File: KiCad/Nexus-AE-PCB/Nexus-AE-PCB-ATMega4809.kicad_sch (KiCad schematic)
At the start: 1 part, among them U1 ATmega4809-A

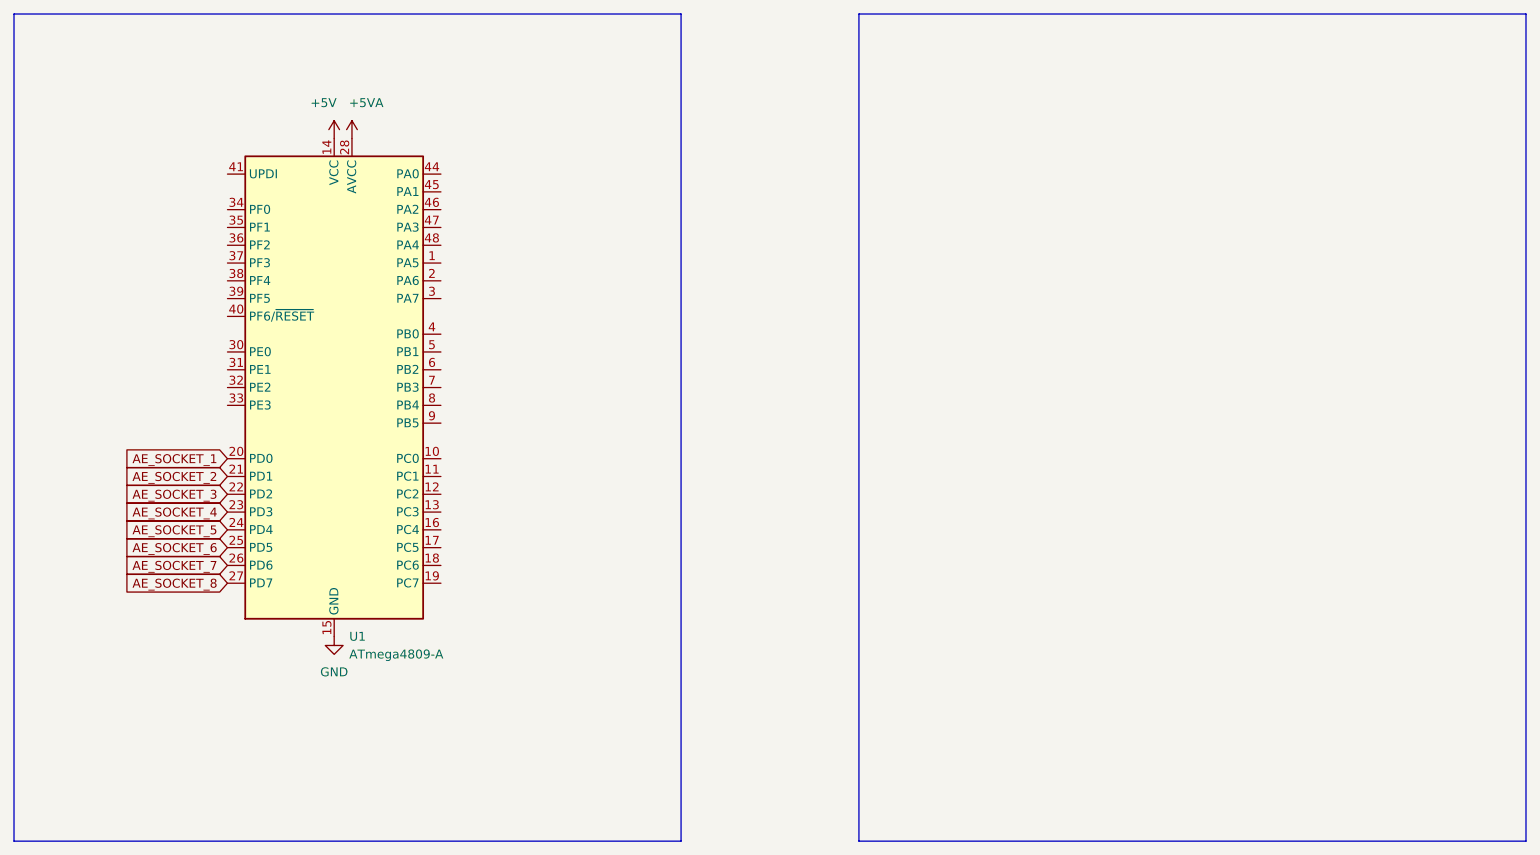
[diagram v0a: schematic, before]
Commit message: PCB and schmeatic are both approx 90% complete
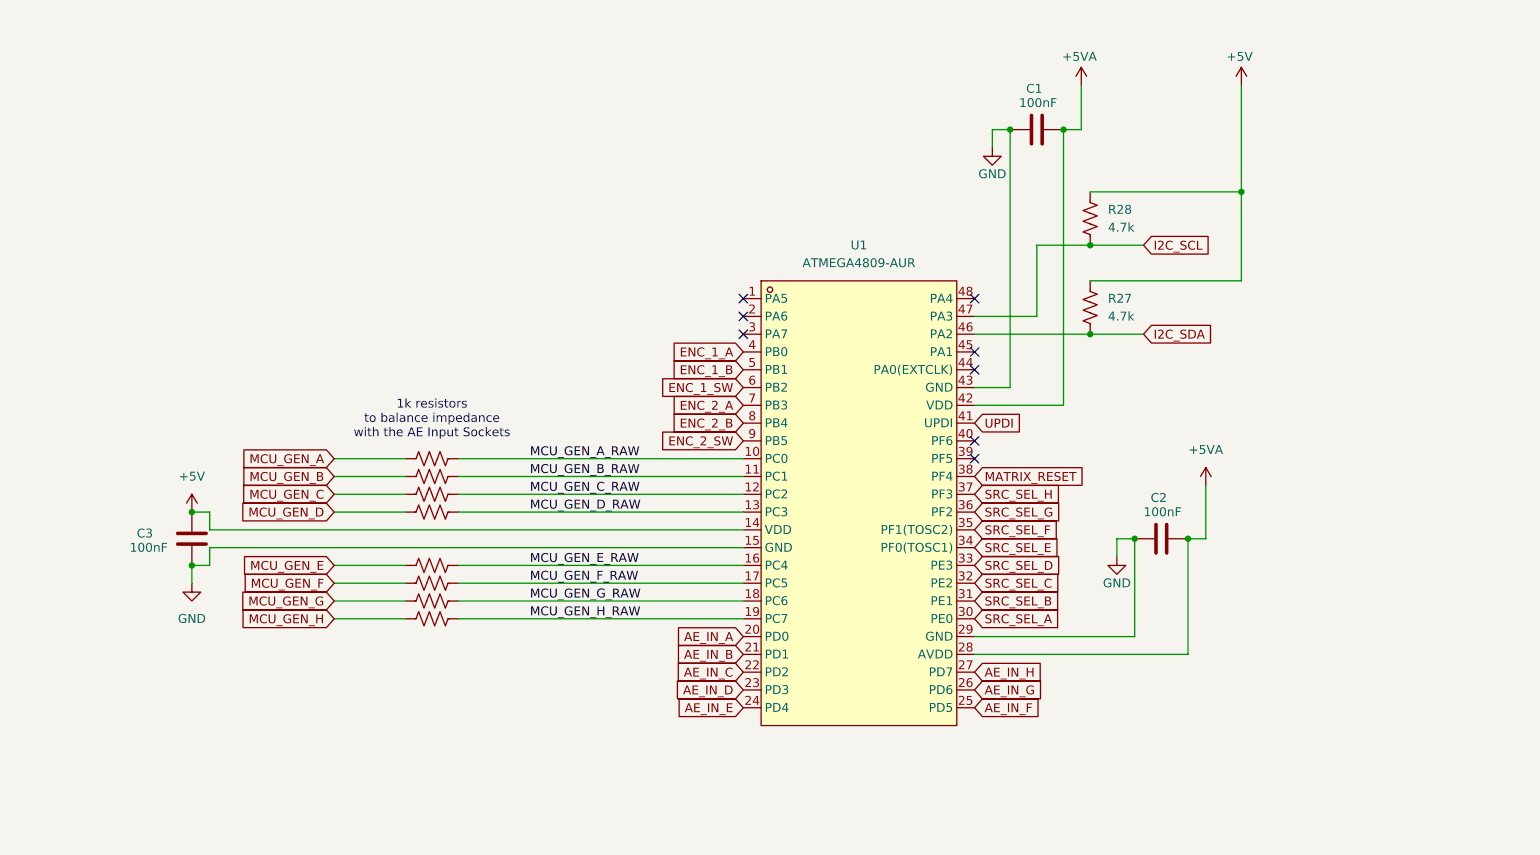
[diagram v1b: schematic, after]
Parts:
- removed U1: ATmega4809-A, Package_QFP:TQFP-48_7x7mm_P0.5mm, symbol MCU_Microchip_ATmega:ATmega4809-A
- added C1, C2, C3: 100nF, Capacitor_SMD:C_0402_1005Metric, symbol Device:C
- added R27, R28: 4.7k, Resistor_SMD:R_0402_1005Metric, symbol Device:R_US
- added R29, R30, R31, R32, R33, R34, R35, R36: 1k, Resistor_SMD:R_0402_1005Metric, symbol Device:R_US
- added U1: ATMEGA4809-AUR, clectric-diy:TQFP-48_L7.0-W7.0-P0.50-LS9.0-BL, symbol clectric-diy:ATMEGA4809-AUR
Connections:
- net +5V: now also C3.2, R27.1, R28.1, U1.14 (VDD)
- net +5VA: now also C1.2, C2.2, U1.28 (AVDD), U1.42 (VDD)
- net GND: now also C1.1, C2.1, C3.1, U1.15 (GND), U1.29 (GND), U1.43 (GND)
- new net AE_IN_A: U1.20 (PD0)
- new net AE_IN_B: U1.21 (PD1)
- new net AE_IN_C: U1.22 (PD2)
- new net AE_IN_D: U1.23 (PD3)
- new net AE_IN_E: U1.24 (PD4)
- new net AE_IN_F: U1.25 (PD5)
- new net AE_IN_G: U1.26 (PD6)
- new net AE_IN_H: U1.27 (PD7)
- new net ENC_1_A: U1.4 (PB0)
- new net ENC_1_B: U1.5 (PB1)
- new net ENC_1_SW: U1.6 (PB2)
- new net ENC_2_A: U1.7 (PB3)
- new net ENC_2_B: U1.8 (PB4)
- new net ENC_2_SW: U1.9 (PB5)
- new net I2C_SCL: R28.2, U1.47 (PA3)
- new net I2C_SDA: R27.2, U1.46 (PA2)
- new net MATRIX_RESET: U1.38 (PF4)
- new net MCU_GEN_A: R29.1
- new net MCU_GEN_A_RAW: R29.2, U1.10 (PC0)
- new net MCU_GEN_B: R30.1
- new net MCU_GEN_B_RAW: R30.2, U1.11 (PC1)
- new net MCU_GEN_C: R31.1
- new net MCU_GEN_C_RAW: R31.2, U1.12 (PC2)
- new net MCU_GEN_D: R32.1
- new net MCU_GEN_D_RAW: R32.2, U1.13 (PC3)
- new net MCU_GEN_E: R33.1
- new net MCU_GEN_E_RAW: R33.2, U1.16 (PC4)
- new net MCU_GEN_F: R34.1
- new net MCU_GEN_F_RAW: R34.2, U1.17 (PC5)
- new net MCU_GEN_G: R35.1
- new net MCU_GEN_G_RAW: R35.2, U1.18 (PC6)
- new net MCU_GEN_H: R36.1
- new net MCU_GEN_H_RAW: R36.2, U1.19 (PC7)
- new net SRC_SEL_A: U1.30 (PE0)
- new net SRC_SEL_B: U1.31 (PE1)
- new net SRC_SEL_C: U1.32 (PE2)
- new net SRC_SEL_D: U1.33 (PE3)
- new net SRC_SEL_E: U1.34 (PF0(TOSC1))
- new net SRC_SEL_F: U1.35 (PF1(TOSC2))
- new net SRC_SEL_G: U1.36 (PF2)
- new net SRC_SEL_H: U1.37 (PF3)
- new net UPDI: U1.41 (UPDI)
- no-connect marks 0 -> 8
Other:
- note added: "1k resistors to balance impedance with the AE Input Sockets"
